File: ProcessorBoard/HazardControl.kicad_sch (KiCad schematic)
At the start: 7 parts, among them U14 ATF22V10C-7PX, U15 ATF22V10C-7PX

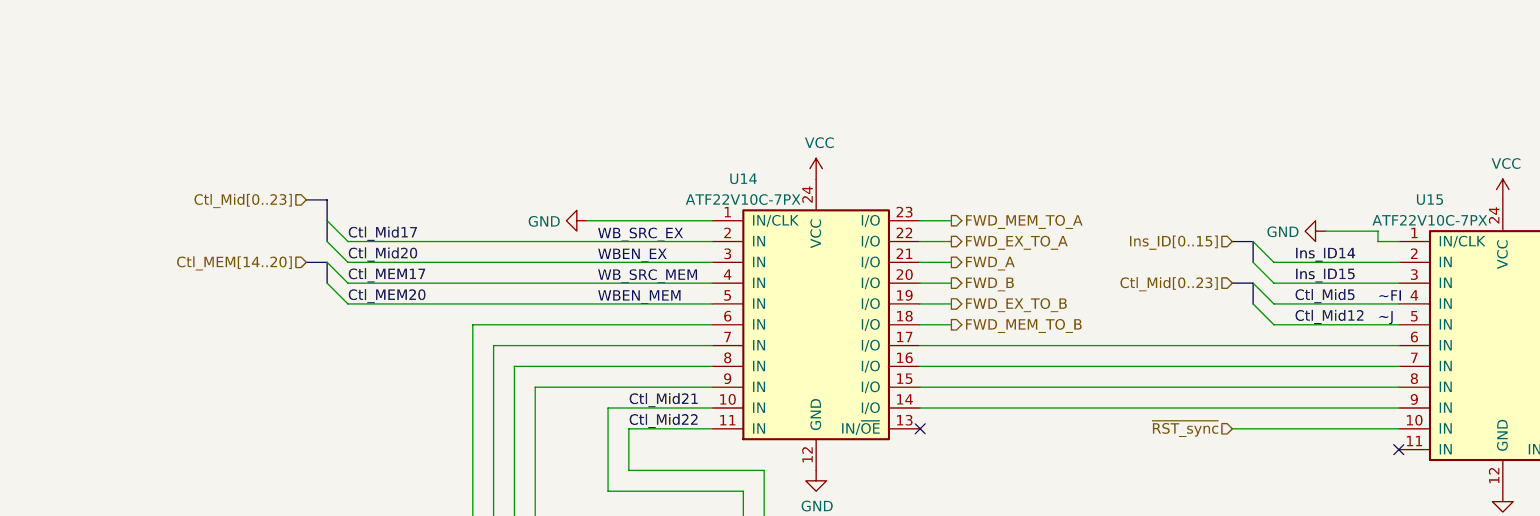
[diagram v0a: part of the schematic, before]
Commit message: ProcessorBoard: Update with changes to Control module Ctl_Mid/Ctl_EX issue
This fixes the second issue in Rev D with Ctl_Mid/Ctl_EX.

Two more signals in Hazard Control were using signals from Ctl_Mid when
they should have instead been using signals from Ctl_EX. This fixes an
issue where the control module is unable to correctly detect a RAW hazard
in the EX stage.
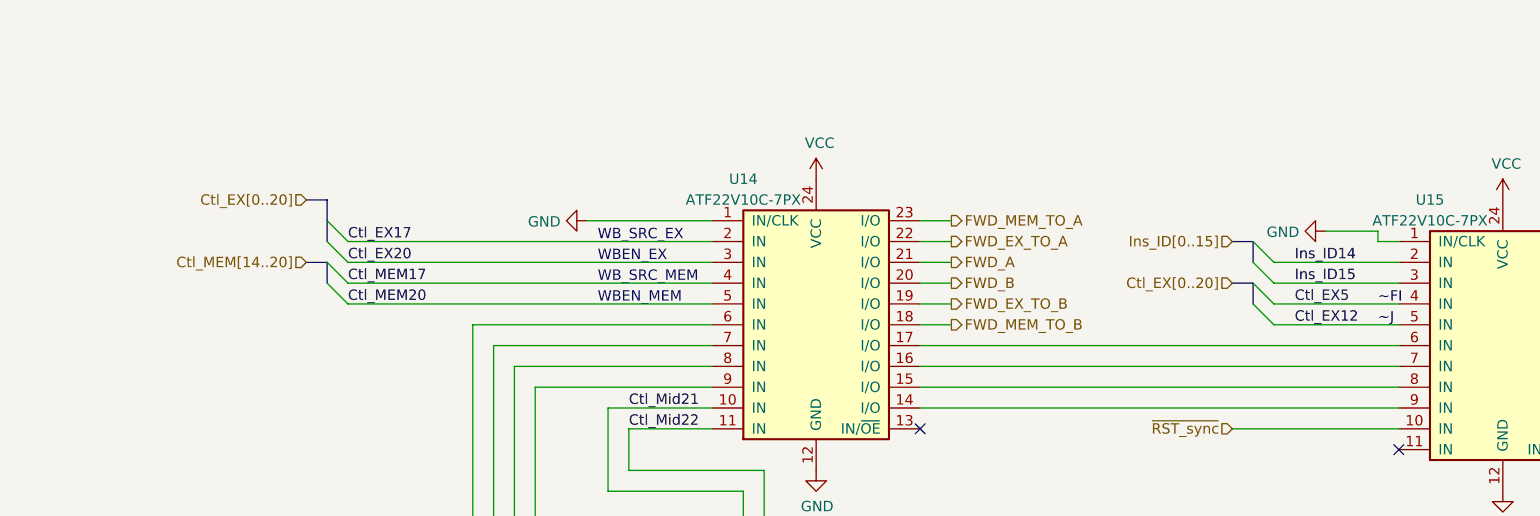
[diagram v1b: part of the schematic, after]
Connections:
- net Ctl_Mid12 renamed Ctl_EX12
- net Ctl_Mid17 renamed Ctl_EX17
- net Ctl_Mid20 renamed Ctl_EX20
- net Ctl_Mid5 renamed Ctl_EX5
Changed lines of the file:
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@@
   (title_block
     (title "Hazard Control")
-    (date "2023-11-15")
+    (date "2023-11-19")
     (rev "A")
     (comment 2 "control operand forwarding.")
@@
     (effects (font (size 1.27 1.27)) (justify left bottom))
   )
-  (label "Ctl_Mid12" (at 199.39 93.98 0) (fields_autoplaced)
+  (label "Ctl_EX12" (at 199.39 93.98 0) (fields_autoplaced)
     (effects (font (size 1.27 1.27)) (justify left bottom))
   )
@@
     (effects (font (size 1.27 1.27)) (justify left bottom))
   )
-  (label "Ctl_Mid5" (at 199.39 91.44 0) (fields_autoplaced)
+  (label "Ctl_EX5" (at 199.39 91.44 0) (fields_autoplaced)
     (effects (font (size 1.27 1.27)) (justify left bottom))
   )
@@
     (effects (font (size 1.27 1.27)) (justify left bottom))
   )
-  (label "Ctl_Mid17" (at 83.82 83.82 0) (fields_autoplaced)
+  (label "Ctl_EX17" (at 83.82 83.82 0) (fields_autoplaced)
     (effects (font (size 1.27 1.27)) (justify left bottom))
   )
@@
     (effects (font (size 1.27 1.27)) (justify left bottom))
   )
-  (label "Ctl_Mid20" (at 83.82 86.36 0) (fields_autoplaced)
+  (label "Ctl_EX20" (at 83.82 86.36 0) (fields_autoplaced)
     (effects (font (size 1.27 1.27)) (justify left bottom))
   )
@@
     (effects (font (size 1.27 1.27)) (justify right))
   )
-  (hierarchical_label "Ctl_Mid[0..23]" (shape input) (at 191.77 88.9 180) (fields_autoplaced)
+  (hierarchical_label "Ctl_EX[0..20]" (shape input) (at 191.77 88.9 180) (fields_autoplaced)
     (effects (font (size 1.27 1.27)) (justify right))
   )
@@
     (effects (font (size 1.27 1.27)) (justify left))
   )
-  (hierarchical_label "Ctl_Mid[0..23]" (shape input) (at 78.74 78.74 180) (fields_autoplaced)
-    (effects (font (size 1.27 1.27)) (justify right))
-  )
+  (hierarchical_label "Ctl_EX[0..20]" (shape input) (at 78.74 78.74 180) (fields_autoplaced)
+    (effects (font (size 1.27 1.27)) (justify right))
+  )

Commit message: ProcessorBoard: Copy symbols into project symbol library, make consistent
Symbols created for Turtle16 have been copied into a project-specific
symbol library. The symbols have all been updated with manufacturer,
manufacturer part number, mouser part number, and digikey part number.

Test points and mounting holes have been marked to be excluded from BOM.
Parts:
- C15, C16: footprint Capacitor_SMD:C_0603_1608Metric_Pad1.08x0.95mm_HandSolder -> Capacitor_SMD:C_0603_1608Metric; Digikey# (none) -> 587-6004-1-ND; Manufacturer (none) -> Taiyo Yuden; Manufacturer# (none) -> EMK107B7104KAHT; Mouser https://www.mouser.com/ProductDetail/963-EMK107B7104KAHT -> (none); Mouser# (none) -> 963-EMK107B7104KAHT
- TP28, TP29, TP30: now left out of the parts list
- U14, U15: symbol ControlModule-rescue:ATF22V10C-Logic_Programmable -> Turtle16:ATF22V10C; Digikey# (none) -> ATF22V10C-7PX-ND; Manufacturer (none) -> Microchip Technology; Manufacturer# (none) -> ATF22V10C-7PX; Mouser https://www.mouser.com/ProductDetail/Microchip-Technology-A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 -> (none); Mouser# (none) -> 556-AF22V10C7PX
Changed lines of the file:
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@@
   (title_block
     (title "Hazard Control")
-    (date "2023-11-20")
+    (date "2023-11-25")
     (rev "A")
     (comment 2 "control operand forwarding.")
@@
     )
   )
-  (symbol (lib_id "ControlModule-rescue:ATF22V10C-Logic_Programmable") (at 140.97 92.71 0) (unit 1)
+  (symbol (lib_id "Turtle16:ATF22V10C") (at 140.97 92.71 0) (unit 1)
     (in_bom yes) (on_board yes) (dnp no)
     (property "Reference" "U14" (at 132.08 76.2 0)
@@
       (effects (font (size 1.27 1.27)) hide)
     )
-    (property "Mouser" "https://www.mouser.com/ProductDetail/Microchip-Technology-Atmel/ATF22V10C-7PX?qs=%2Fha2pyFadugqFuTUlWvkuaZr7DXQ8Rnu3dOZcKuoHGuPC51te6MYUw%3D%3D" (at 140.97 92.71 0)
+    (property "Manufacturer" "Microchip Technology" (at 140.97 92.71 0)
+      (effects (font (size 1.27 1.27)) hide)
+    )
+    (property "Manufacturer#" "ATF22V10C-7PX" (at 140.97 92.71 0)
+      (effects (font (size 1.27 1.27)) hide)
+    )
+    (property "Mouser#" "556-AF22V10C7PX" (at 140.97 92.71 0)
+      (effects (font (size 1.27 1.27)) hide)
+    )
+    (property "Digikey#" "ATF22V10C-7PX-ND" (at 140.97 92.71 0)
       (effects (font (size 1.27 1.27)) hide)
     )
@@
       (effects (font (size 1.27 1.27)) (justify left))
     )
-    (property "Footprint" "Capacitor_SMD:C_0603_1608Metric_Pad1.08x0.95mm_HandSolder" (at 17.4752 194.31 0)
-      (effects (font (size 1.27 1.27)) hide)
-    )
-    (property "Datasheet" "~" (at 16.51 190.5 0)
-      (effects (font (size 1.27 1.27)) hide)
-    )
-    (property "Mouser" "https://www.mouser.com/ProductDetail/963-EMK107B7104KAHT" (at 16.51 190.5 0)
+    (property "Footprint" "Capacitor_SMD:C_0603_1608Metric" (at 128.5748 82.55 0)
+      (effects (font (size 1.27 1.27)) hide)
+    )
+    (property "Datasheet" "https://www.mouser.com/datasheet/2/396/taiyo_yuden_12132018_mlcc11_hq_e-1510082.pdf" (at 129.54 78.74 0)
+      (effects (font (size 1.27 1.27)) hide)
+    )
+    (property "Manufacturer" "Taiyo Yuden" (at 129.54 78.74 0)
+      (effects (font (size 1.27 1.27)) hide)
+    )
+    (property "Manufacturer#" "EMK107B7104KAHT" (at 129.54 78.74 0)
+      (effects (font (size 1.27 1.27)) hide)
+    )
+    (property "Mouser#" "963-EMK107B7104KAHT" (at 129.54 78.74 0)
+      (effects (font (size 1.27 1.27)) hide)
+    )
+    (property "Digikey#" "587-6004-1-ND" (at 129.54 78.74 0)
       (effects (font (size 1.27 1.27)) hide)
     )
@@
       (effects (font (size 1.27 1.27)) (justify left))
     )
-    (property "Footprint" "Capacitor_SMD:C_0603_1608Metric_Pad1.08x0.95mm_HandSolder" (at 30.1752 194.31 0)
-      (effects (font (size 1.27 1.27)) hide)
-    )
-    (property "Datasheet" "~" (at 29.21 190.5 0)
-      (effects (font (size 1.27 1.27)) hide)
-    )
-    (property "Mouser" "https://www.mouser.com/ProductDetail/963-EMK107B7104KAHT" (at 29.21 190.5 0)
+    (property "Footprint" "Capacitor_SMD:C_0603_1608Metric" (at 128.5748 82.55 0)
+      (effects (font (size 1.27 1.27)) hide)
+    )
+    (property "Datasheet" "https://www.mouser.com/datasheet/2/396/taiyo_yuden_12132018_mlcc11_hq_e-1510082.pdf" (at 129.54 78.74 0)
+      (effects (font (size 1.27 1.27)) hide)
+    )
+    (property "Manufacturer" "Taiyo Yuden" (at 129.54 78.74 0)
+      (effects (font (size 1.27 1.27)) hide)
+    )
+    (property "Manufacturer#" "EMK107B7104KAHT" (at 129.54 78.74 0)
+      (effects (font (size 1.27 1.27)) hide)
+    )
+    (property "Mouser#" "963-EMK107B7104KAHT" (at 129.54 78.74 0)
+      (effects (font (size 1.27 1.27)) hide)
+    )
+    (property "Digikey#" "587-6004-1-ND" (at 129.54 78.74 0)
       (effects (font (size 1.27 1.27)) hide)
     )
@@
     )
   )
-  (symbol (lib_id "ControlModule-rescue:ATF22V10C-Logic_Programmable") (at 224.79 95.25 0) (unit 1)
+  (symbol (lib_id "Turtle16:ATF22V10C") (at 224.79 95.25 0) (unit 1)
     (in_bom yes) (on_board yes) (dnp no)
     (property "Reference" "U15" (at 215.9 78.74 0)
@@
       (effects (font (size 1.27 1.27)) hide)
     )
-    (property "Mouser" "https://www.mouser.com/ProductDetail/Microchip-Technology-Atmel/ATF22V10C-7PX?qs=%2Fha2pyFadugqFuTUlWvkuaZr7DXQ8Rnu3dOZcKuoHGuPC51te6MYUw%3D%3D" (at 224.79 95.25 0)
+    (property "Manufacturer" "Microchip Technology" (at 224.79 95.25 0)
+      (effects (font (size 1.27 1.27)) hide)
+    )
+    (property "Manufacturer#" "ATF22V10C-7PX" (at 224.79 95.25 0)
+      (effects (font (size 1.27 1.27)) hide)
+    )
+    (property "Mouser#" "556-AF22V10C7PX" (at 224.79 95.25 0)
+      (effects (font (size 1.27 1.27)) hide)
+    )
+    (property "Digikey#" "ATF22V10C-7PX-ND" (at 224.79 95.25 0)
       (effects (font (size 1.27 1.27)) hide)
     )
@@
   )
   (symbol (lib_id "Connector:TestPoint") (at 254.635 77.47 0) (unit 1)
-    (in_bom yes) (on_board yes) (dnp no) (fields_autoplaced)
+    (in_bom no) (on_board yes) (dnp no) (fields_autoplaced)
     (property "Reference" "TP30" (at 256.54 72.898 0)
       (effects (font (size 1.27 1.27)) (justify left))
@@
   )
   (symbol (lib_id "Connector:TestPoint") (at 252.095 70.485 0) (unit 1)
-    (in_bom yes) (on_board yes) (dnp no) (fields_autoplaced)
+    (in_bom no) (on_board yes) (dnp no) (fields_autoplaced)
     (property "Reference" "TP29" (at 254 65.9129 0)
       (effects (font (size 1.27 1.27)) (justify left))
@@
   )
   (symbol (lib_id "Connector:TestPoint") (at 249.555 64.135 0) (unit 1)
-    (in_bom yes) (on_board yes) (dnp no) (fields_autoplaced)
+    (in_bom no) (on_board yes) (dnp no) (fields_autoplaced)
     (property "Reference" "TP28" (at 251.46 59.5629 0)
       (effects (font (size 1.27 1.27)) (justify left))
